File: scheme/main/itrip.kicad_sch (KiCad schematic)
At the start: 15 parts

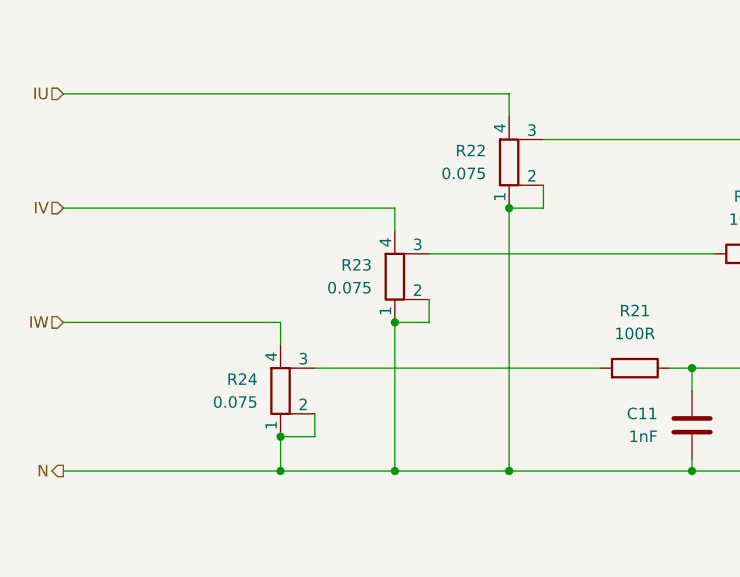
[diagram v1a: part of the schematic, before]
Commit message: control isolation schematic
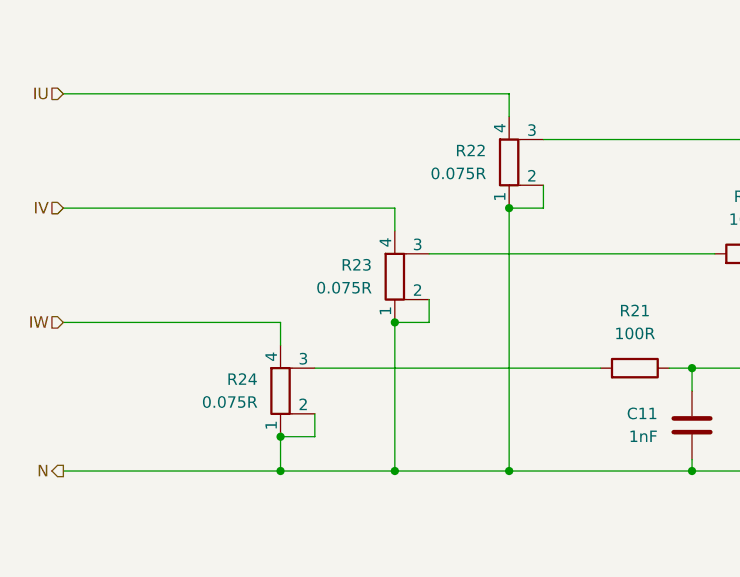
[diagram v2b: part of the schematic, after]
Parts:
- R22, R23, R24: value 0.075 -> 0.075R
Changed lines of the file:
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@@
 			)
 		)
-		(property "Value" "0.075"
+		(property "Value" "0.075R"
 			(at 64.77 116.8399 0)
 			(effects
@@
 			)
 		)
-		(property "Value" "0.075"
+		(property "Value" "0.075R"
 			(at 77.47 104.1399 0)
 			(effects
@@
 			)
 		)
-		(property "Value" "0.075"
+		(property "Value" "0.075R"
 			(at 90.17 91.4399 0)
 			(effects

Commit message: separate hi power & signal gnd
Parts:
- added NT2: NetTie_2, symbol Device:NetTie_2
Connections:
- net N is gone; now on net GNDPWR: C10.2, C11.2, C2.2, R22.1, R22.2, R23.1, R23.2, R24.1, R24.2
- net GNDPWR: now also NT2.1; no longer C1.2, R3.1
- new net GNDH: C1.2, NT2.2, R3.1
